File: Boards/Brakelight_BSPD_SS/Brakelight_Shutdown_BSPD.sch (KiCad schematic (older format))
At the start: 73 parts, among them IC1 ATMEGA16M1, J2 MM_F_RA_20, J3 CONN_02X03, Q1 SSM3K333R, Q2 SSM3K333R, Q6 SSM3K333R, U1 SN74LVC1G08, U101 TPS560430YF, U2 MCP6001, U3 CAN_Transceiver, U4 MCP6001, U5 SN74LVC1G02, U6 SN74LVC1G02, U7 MCP6001, U8 SN74LVC1G32, Y1 Crystal_SMD

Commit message: Finished schematic
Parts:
- removed D11: LED_0805, footprints:LED_0805_OEM, symbol formula:LED_0805
- removed R59: R_200, footprints:R_0805_OEM, symbol formula:R_200
- added C11, C7: C_1uF, footprints:C_0805_OEM, symbol formula:C_1uF
- added D2: LED_0805, footprints:LED_0805_OEM, symbol formula:LED_0805
- added Q3: SSM3K333R, footprints:SOT-23F, symbol formula:SSM3K333R
- added R2, R20, R21, R23: R_10K, footprints:R_0805_OEM, symbol formula:R_10K
- added R22: R_100K, footprints:R_0805_OEM, symbol formula:R_100K
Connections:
- net GND: now also J2.12, J2.20, C11.2, C7.2, D2.1 (K), Q3.2 (S), R22.1; no longer J2.17
- net MISO: now also J2.4; no longer J2.9
- net MOSI: now also J2.5; no longer J2.10
- net RESET: now also J2.7; no longer J2.12
- net SCK: now also J2.6; no longer J2.11
- net VCC: now also J2.10, J2.3, R23.1; no longer J2.15, J2.8
- net SHUTDOWN_SENSE_BSPD_PIN: now reaches IC1.25 ((PCINT15/D2A/AMP2+)PC7)
- net SHUTDOWN_SENSE_BSPD_PIN: now also Q3.3 (D), R23.2
- net at U7.1: now also R20.2; no longer U8.2 (in)
- net at U4.1: now also R2.2; no longer U8.1 (in)
- net BSPD_Current_Sense renamed BSPD_CURRENT_SENSE
- net BSPD_CURRENT_SENSE: now also J2.14, J2.19; no longer J2.18
- net BSPD_Relay renamed BSPD_RELAY_LSD
- net BSPD_RELAY_LSD: now also J2.17; no longer J2.3
- net BSPD_Relay_Sense renamed BSPD_RELAY_SENSE
- net Brake_Pressure_Sense renamed BRAKE_PRESSURE_SENSE
- net BRAKE_PRESSURE_SENSE: now also J2.11; no longer J2.16
- net Brakelight_Gate renamed BRAKELIGHT_GATE
- net Brakelight_LSD renamed BRAKELIGHT_LSD
- net BRAKELIGHT_LSD: now also J2.13; no longer J2.14
- net CAN_high renamed CAN_HIGH
- net CAN_HIGH: now also J2.8; no longer J2.6
- net CAN_low renamed CAN_LOW
- net CAN_LOW: now also J2.9; no longer J2.7
- net Cooling_Pump_LSD: no longer names the net of IC1.30 ((PCINT8/INT3/PSCOUT1A)PC0)
- net Cooling_Pump_LSD: no longer J2.13
- net LED_1 renamed DEBUG_LED_1
- net LED_2 renamed DEBUG_LED_2
- net LED_3 renamed DEBUG_LED_3
- net RJ45_LED1 renamed RJ45_LED_G
- net RJ45_LED_G: now also J2.15; no longer J2.19
- net RJ45_LED2 renamed RJ45_LED_0
- net RJ45_LED_0: now also J2.16; no longer J2.20
- new net: C7.1, R2.1, U8.1 (in)
- new net: C11.1, R20.1, U8.2 (in)
- new net: D2.2 (A), R21.2
- new net SHUTDOWN_SENSE_BSPD: J2.18, Q3.1 (G), R21.1, R22.2
- no-connect marks 13 -> 11
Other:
- note added: "Brake_Pressure_Sense is an off board\ncomponent that measures the pressure\nbeing applied to the brakes."
- note added: "CAN Transceiver"
- note added: "Connector"
- note added: "Debugging LEDs"
- note added: "Low pass filters to prevent\nany potential oscillations"
- note added: "Programming Header"
- note added: "Shutdown Sense"
- note added: "When SHUTDOWN_SENSE_BSPD is\nlow (shutdown circuit is OPEN), LED\nwill turn off and CAN message will\nbe sent.\n"
- note removed: "Brake_Pressure_Sense is an off board component \nthat measures the pressure being applied to the brakes."
- moved on the sheet: C10, C5, C6, C8, C9, D1, D12, D13, D4, D5, J2, J3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

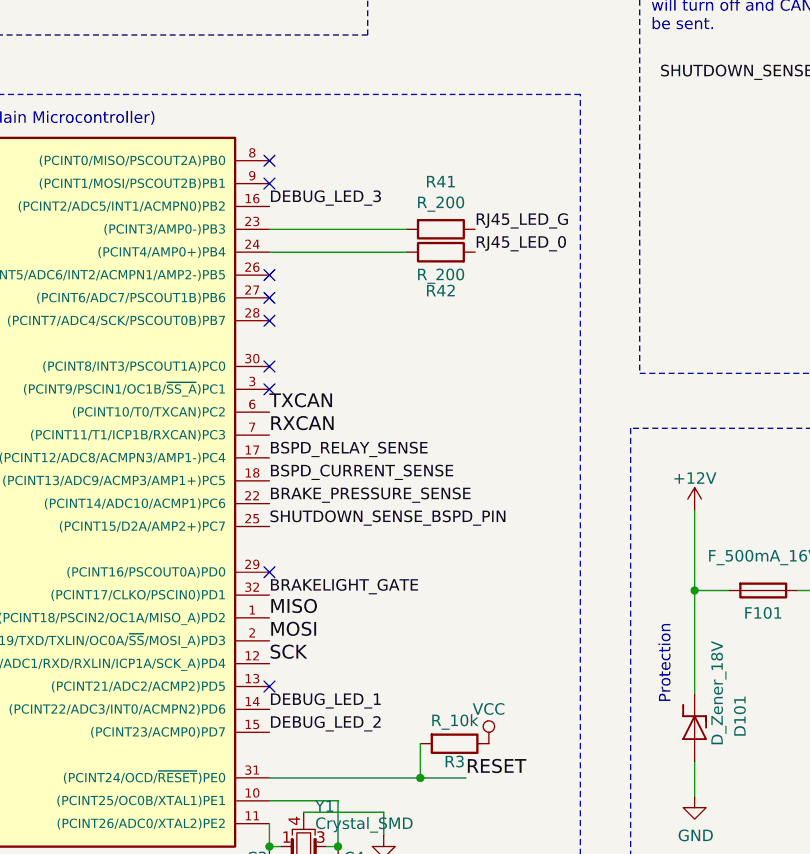
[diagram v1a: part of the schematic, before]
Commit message: Finished PCB layout
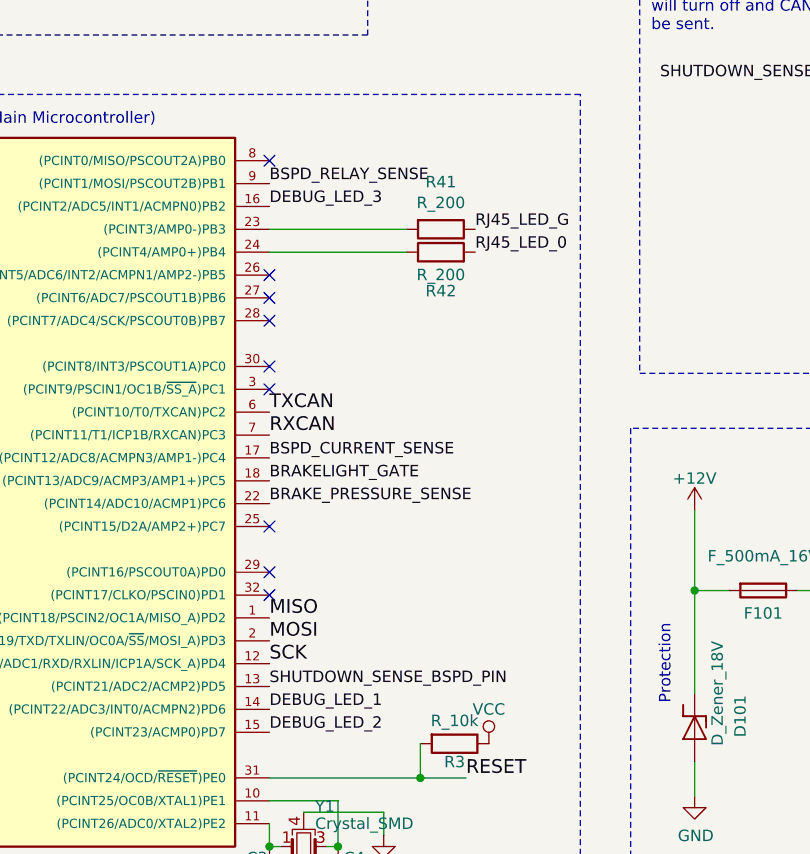
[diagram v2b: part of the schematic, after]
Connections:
- net BRAKELIGHT_GATE: now also IC1.18 ((PCINT13/ADC9/ACMP3/AMP1+)PC5); no longer IC1.32 ((PCINT17/CLKO/PSCIN0)PD1)
- net BSPD_CURRENT_SENSE: now also IC1.17 ((PCINT12/ADC8/ACMPN3/AMP1-)PC4); no longer IC1.18 ((PCINT13/ADC9/ACMP3/AMP1+)PC5)
- net BSPD_RELAY_SENSE: now also IC1.9 ((PCINT1/MOSI/PSCOUT2B)PB1); no longer IC1.17 ((PCINT12/ADC8/ACMPN3/AMP1-)PC4)
- net SHUTDOWN_SENSE_BSPD_PIN: now also IC1.13 ((PCINT21/ADC2/ACMP2)PD5); no longer IC1.25 ((PCINT15/D2A/AMP2+)PC7)
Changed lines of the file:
@@
 	1    0    0    -1
 $EndComp
-Text Label 3450 8250 0    50   ~ 0
+Text Label 3450 8150 0    50   ~ 0
 BSPD_CURRENT_SENSE
 Text Label 3740 2800 2    50   ~ 0
@@
 	3980 2500 3740 2500
 Connection ~ 3980 2500
-Text Label 3450 8750 0    50   ~ 0
-BRAKELIGHT_GATE
 Connection ~ 8390 2610
 Wire Wire Line
@@
 	7430 2670 7430 3210
 NoConn ~ 3450 6850
-NoConn ~ 3450 6950
 Text Label 4350 7250 0    50   ~ 0
 RJ45_LED_0
@@
 Wire Wire Line
 	7380 9920 7380 9950
-Text Label 3450 8150 0    50   ~ 0
-BSPD_RELAY_SENSE
-NoConn ~ 3450 9150
 $Comp
 L power:GND #PWR?
@@
 Wire Wire Line
 	6930 6460 6930 6520
-Text Label 3450 8450 0    50   ~ 0
+Text Label 3450 9150 0    50   ~ 0
 SHUTDOWN_SENSE_BSPD_PIN
 Text Label 1210 6070 0    50   ~ 0
@@
 Text Notes 5120 6290 0    50   ~ 0
 When SHUTDOWN_SENSE_BSPD is\nlow (shutdown circuit is OPEN), LED\nwill turn off and CAN message will\nbe sent.\n
+Text Label 3450 6950 0    50   ~ 0
+BSPD_RELAY_SENSE
+NoConn ~ 3450 8750
+Text Label 3450 8250 0    50   ~ 0
+BRAKELIGHT_GATE
+NoConn ~ 3450 8450
 $EndSCHEMATC

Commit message: Updated layout from 11/2 design review
Added r_0 in before brakelight circuit. Added bypass capacitors
for op amps and OR gates.
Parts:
- removed R14: R_200, footprints:R_0805_OEM, symbol formula:R_200
- added C12, C13, C14: C_0.1uF, footprints:C_0805_OEM, symbol formula:C_0.1uF
- added R14: R_0, footprints:R_0603_1608Metric, symbol formula:R_0
- added R24: R_120_DNP, footprints:R_0805_OEM, symbol formula:R_120_DNP
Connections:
- net BRAKE_PRESSURE_SENSE: now also R14.2; no longer R10.2, U4.4 (-), U7.3 (+)
- net CAN_HIGH: now also R24.1
- net CAN_LOW: now also R24.2
- net GND: now also C12.2, C13.2, C14.2
- net VCC: now also C12.1, C13.1, C14.1
- net BSPD_RELAY_SENSE renamed BSPD_RELAY_INTENTION
- net RJ45_LED_0 renamed RJ45_LED_O
- new net: R10.2, R14.1, U4.4 (-), U7.3 (+)
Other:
- note removed: "DNP R_200\n"
- note removed: "Low pass filters to prevent\nany potential oscillations"
- note removed: "When SHUTDOWN_SENSE_BSPD is\nlow (shutdown circuit is OPEN), LED\nwill turn off and CAN message will\nbe sent.\n"
- moved on the sheet: R10
